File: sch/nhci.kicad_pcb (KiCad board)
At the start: 4 copper layers, 70 parts, among them IC1 74LVC8T245RHLRG4, IC2 74LVC8T245RHLRG4, IC3 74LVC8T245RHLRG4, IC4 74LVC8T245RHLRG4, IC5 74LVC8T245RHLRG4, IC6 MAX3421EEHJ+, IC7 LT3030IFE#TRPBF, J1 CLP-105-02-F-D, SW1 SW_Push_Open, U1 PCMCIA_BOARD, U2 iCE40-HX8K-CT256, U3 N25Q032A13EF440F, U4 LM3526M-H, Y1 ECS-5032MV-120-BM-TR

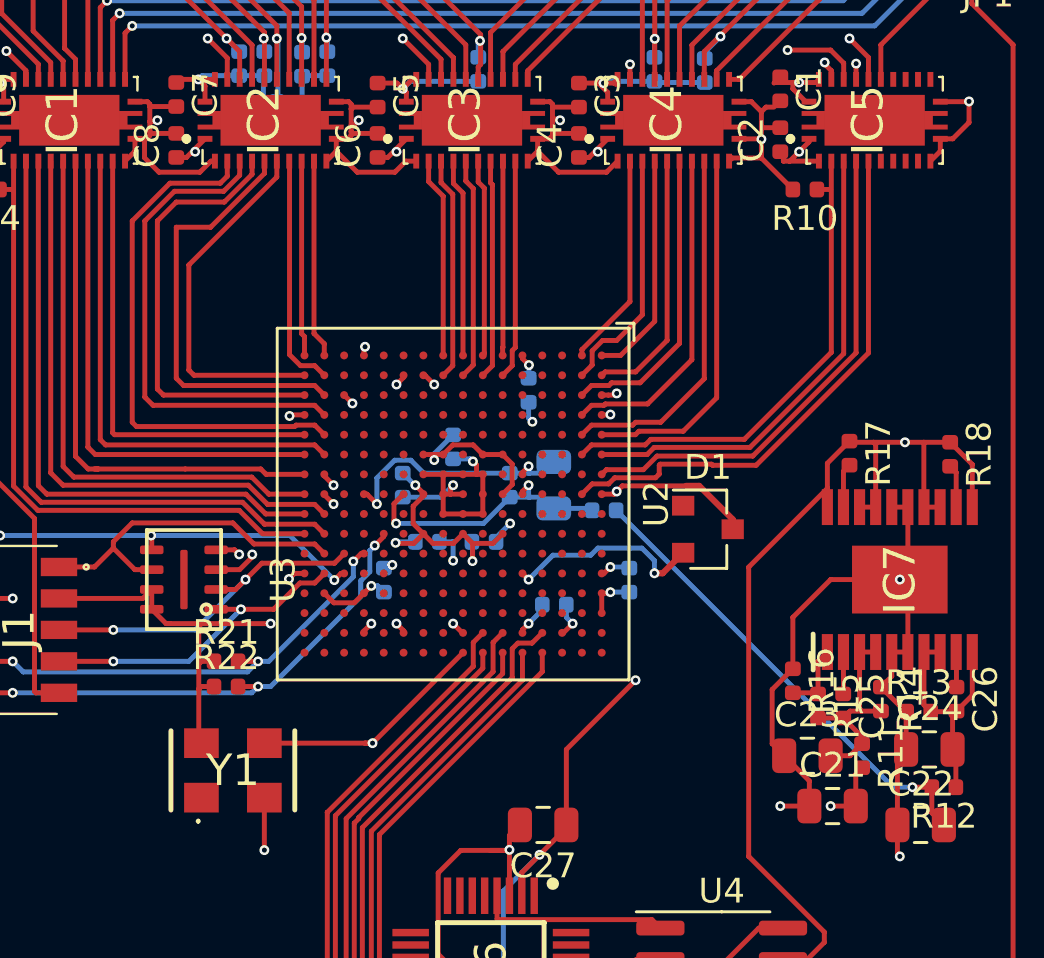
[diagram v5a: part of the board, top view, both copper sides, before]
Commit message: VCC is 1V2 not 3V3
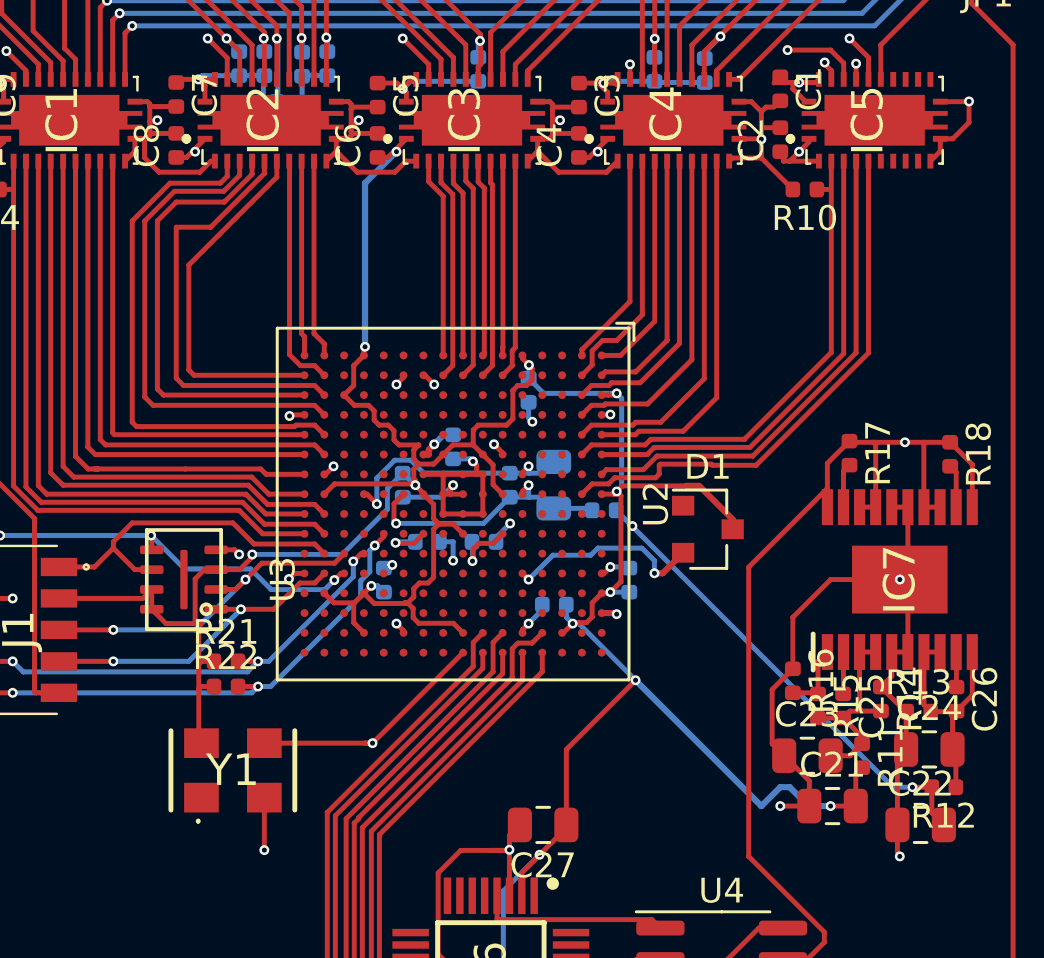
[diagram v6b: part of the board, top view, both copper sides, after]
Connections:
- C18 pad 1: +3V3 -> +1V2
- C19 pad 1: +3V3 -> +1V2
- C20 pad 1: +3V3 -> +1V2
- U2 pad A14: +3V3 -> +1V2
- U2 pad F10: +3V3 -> +1V2
- U2 pad F6: +3V3 -> +1V2
- U2 pad K10: +3V3 -> +1V2
- U2 pad K6: +3V3 -> +1V2
- U2 pad L2: +3V3 -> +1V2
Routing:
- net +3V3: track 137.3 -> 178.8 mm, vias 27 -> 18
- net +1V2: track 19.1 -> 27.4 mm, vias 1 -> 8
- added copper zone on In2.Cu, net +1V2
- removed copper zone on In2.Cu, net +3V3

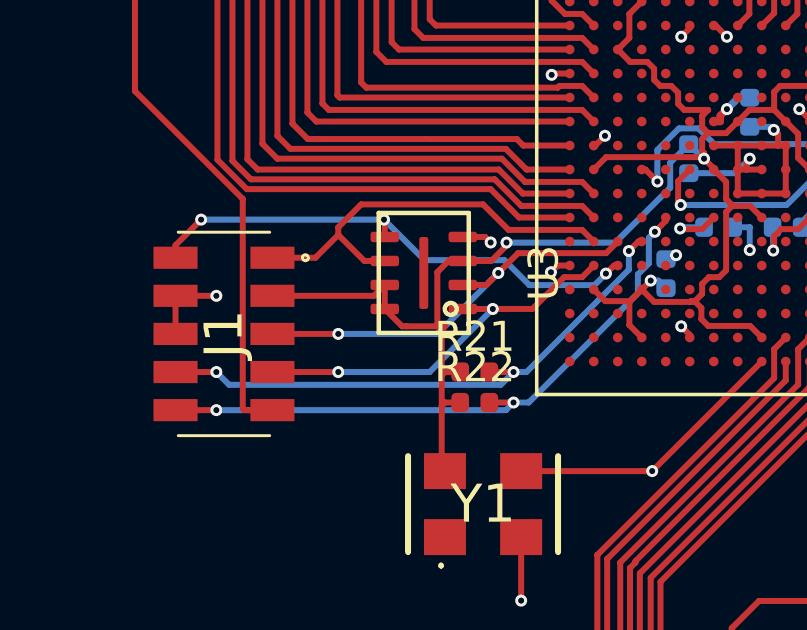
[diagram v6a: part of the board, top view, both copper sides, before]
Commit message: Add recommended SPI pullups
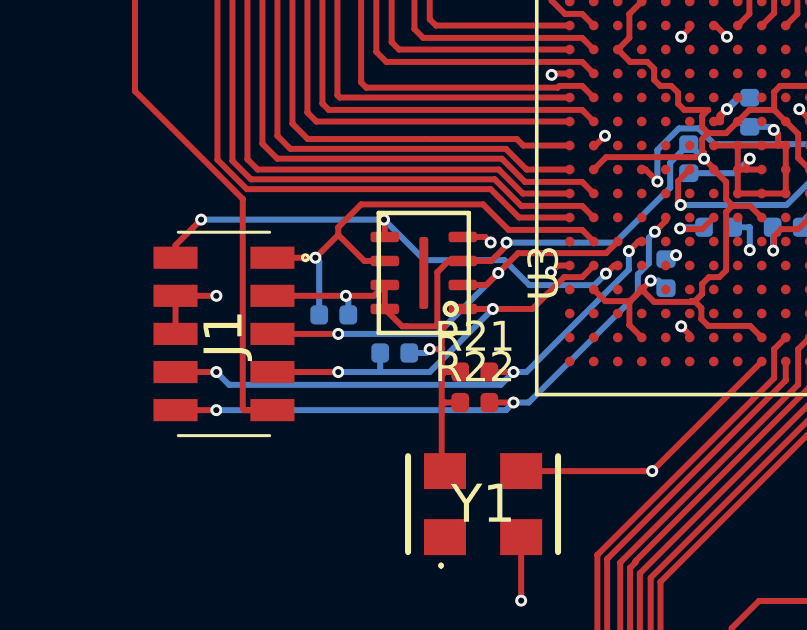
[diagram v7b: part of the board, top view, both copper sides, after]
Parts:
- added R25: 10k, Resistor_SMD:R_0402_1005Metric, B.Cu at (51.4, 128.9)
- added R26: 10k, Resistor_SMD:R_0402_1005Metric, B.Cu at (53.4, 130.2)
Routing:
- net Net-(J1-Pad1): track 14.0 -> 16.0 mm, vias 0 -> 1
- net +3V3: track 178.8 -> 180.6 mm, vias 18 -> 20
- net Net-(J1-Pad7): track 13.2 -> 13.8 mm
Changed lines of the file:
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@@
     (thickness 1.6)
     (drawings 0)
-    (tracks 1274)
+    (tracks 1289)
     (zones 0)
-    (modules 70)
+    (modules 72)
     (nets 370)
   )
@@
     (add_net U_SS)
   )
+  (module Resistor_SMD:R_0402_1005Metric (layer B.Cu)
+    (at 53.444 130.175)
+    (descr "Resistor SMD 0402 (1005 Metric), square (rectangular) end terminal, IPC_7351 nominal, (Body size source: http://www.tortai-tech.com/upload/download/2011102023233369053.pdf), generated with kicad-footprint-generator")
+    (tags resistor)
+    (attr smd)
+    (fp_text reference R26 (at 0 1.17) (layer B.SilkS)
+      (effects (font (size 1 1) (thickness 0.15)) (justify mirror))
+    )
+    (fp_text value 10k (at 0 -1.17) (layer B.Fab)
+      (effects (font (size 1 1) (thickness 0.15)) (justify mirror))
+    )
+    (fp_text user %R (at 0 0) (layer B.Fab)
+      (effects (font (size 0.25 0.25) (thickness 0.04)) (justify mirror))
+    )
+    (fp_line (start -0.5 -0.25) (end -0.5 0.25) (layer B.Fab) (width 0.1))
+    (fp_line (start -0.5 0.25) (end 0.5 0.25) (layer B.Fab) (width 0.1))
+    (fp_line (start 0.5 0.25) (end 0.5 -0.25) (layer B.Fab) (width 0.1))
+    (fp_line (start 0.5 -0.25) (end -0.5 -0.25) (layer B.Fab) (width 0.1))
+    (fp_line (start -0.93 -0.47) (end -0.93 0.47) (layer B.CrtYd) (width 0.05))
+    (fp_line (start -0.93 0.47) (end 0.93 0.47) (layer B.CrtYd) (width 0.05))
+    (fp_line (start 0.93 0.47) (end 0.93 -0.47) (layer B.CrtYd) (width 0.05))
+    (fp_line (start 0.93 -0.47) (end -0.93 -0.47) (layer B.CrtYd) (width 0.05))
+    (pad 2 smd roundrect (at 0.485 0) (size 0.59 0.64) (layers B.Cu B.Paste B.Mask) (roundrect_rratio 0.25)
+      (net 102 +3V3))
+    (pad 1 smd roundrect (at -0.485 0) (size 0.59 0.64) (layers B.Cu B.Paste B.Mask) (roundrect_rratio 0.25)
+      (net 350 "Net-(J1-Pad7)"))
+    (model ${KISYS3DMOD}/Resistor_SMD.3dshapes/R_0402_1005Metric.wrl
+      (at (xyz 0 0 0))
+      (scale (xyz 1 1 1))
+      (rotate (xyz 0 0 0))
+    )
+  )
+  (module Resistor_SMD:R_0402_1005Metric (layer B.Cu)
+    (at 51.412 128.905)
+    (descr "Resistor SMD 0402 (1005 Metric), square (rectangular) end terminal, IPC_7351 nominal, (Body size source: http://www.tortai-tech.com/upload/download/2011102023233369053.pdf), generated with kicad-footprint-generator")
+    (tags resistor)
+    (attr smd)
+    (fp_text reference R25 (at 0 1.17) (layer B.SilkS)
+      (effects (font (size 1 1) (thickness 0.15)) (justify mirror))
+    )
+    (fp_text value 10k (at 0 -1.17) (layer B.Fab)
+      (effects (font (size 1 1) (thickness 0.15)) (justify mirror))
+    )
+    (fp_text user %R (at 0 0) (layer B.Fab)
+      (effects (font (size 0.25 0.25) (thickness 0.04)) (justify mirror))
+    )
+    (fp_line (start -0.5 -0.25) (end -0.5 0.25) (layer B.Fab) (width 0.1))
+    (fp_line (start -0.5 0.25) (end 0.5 0.25) (layer B.Fab) (width 0.1))
+    (fp_line (start 0.5 0.25) (end 0.5 -0.25) (layer B.Fab) (width 0.1))
+    (fp_line (start 0.5 -0.25) (end -0.5 -0.25) (layer B.Fab) (width 0.1))
+    (fp_line (start -0.93 -0.47) (end -0.93 0.47) (layer B.CrtYd) (width 0.05))
+    (fp_line (start -0.93 0.47) (end 0.93 0.47) (layer B.CrtYd) (width 0.05))
+    (fp_line (start 0.93 0.47) (end 0.93 -0.47) (layer B.CrtYd) (width 0.05))
+    (fp_line (start 0.93 -0.47) (end -0.93 -0.47) (layer B.CrtYd) (width 0.05))
+    (pad 2 smd roundrect (at 0.485 0) (size 0.59 0.64) (layers B.Cu B.Paste B.Mask) (roundrect_rratio 0.25)
+      (net 102 +3V3))
+    (pad 1 smd roundrect (at -0.485 0) (size 0.59 0.64) (layers B.Cu B.Paste B.Mask) (roundrect_rratio 0.25)
+      (net 353 "Net-(J1-Pad1)"))
+    (model ${KISYS3DMOD}/Resistor_SMD.3dshapes/R_0402_1005Metric.wrl
+      (at (xyz 0 0 0))
+      (scale (xyz 1 1 1))
+      (rotate (xyz 0 0 0))
+    )
+  )
   (module Package_TO_SOT_SMD:SOT-23 (layer F.Cu)
     (at 75.565 125.476)
@@
   (segment (start 55.118 134.112) (end 55.00999 134.00399) (width 0.2) (layer F.Cu) (net 102))
   (segment (start 52.75 128.27) (end 53.112 127.908) (width 0.2) (layer F.Cu) (net 102))
-  (segment (start 49.367 128.27) (end 52.75 128.27) (width 0.2) (layer F.Cu) (net 102))
   (segment (start 55.118 130.81) (end 55.00999 130.91801) (width 0.2) (layer F.Cu) (net 102))
   (segment (start 55.626 130.81) (end 55.118 130.81) (width 0.2) (layer F.Cu) (net 102))
-  (segment (start 55.00999 130.91801) (end 55.00999 129.39401) (width 0.2) (layer F.Cu) (net 102))
   (segment (start 55.626 131.826) (end 55.118 131.826) (width 0.2) (layer F.Cu) (net 102))
   (segment (start 55.118 131.826) (end 55.00999 131.93401) (width 0.2) (layer F.Cu) (net 102))
@@
   (segment (start 70.358 129.286) (end 70.104 129.286) (width 0.2) (layer B.Cu) (net 102))
   (segment (start 72.644 131.572) (end 70.358 129.286) (width 0.2) (layer B.Cu) (net 102))
+  (via (at 51.816 128.27) (size 0.4) (drill 0.2) (layers F.Cu B.Cu) (net 102))
+  (segment (start 51.897 128.351) (end 51.816 128.27) (width 0.2) (layer B.Cu) (net 102))
+  (segment (start 51.897 128.905) (end 51.897 128.351) (width 0.2) (layer B.Cu) (net 102))
+  (segment (start 49.367 128.27) (end 51.816 128.27) (width 0.2) (layer F.Cu) (net 102))
+  (segment (start 51.816 128.27) (end 52.75 128.27) (width 0.2) (layer F.Cu) (net 102))
+  (via (at 54.61 130.048) (size 0.4) (drill 0.2) (layers F.Cu B.Cu) (net 102))
+  (segment (start 53.929 130.175) (end 54.483 130.175) (width 0.2) (layer B.Cu) (net 102))
+  (segment (start 54.483 130.175) (end 54.61 130.048) (width 0.2) (layer B.Cu) (net 102))
+  (segment (start 54.991 130.048) (end 55.00999 130.02901) (width 0.2) (layer F.Cu) (net 102))
+  (segment (start 54.61 130.048) (end 54.991 130.048) (width 0.2) (layer F.Cu) (net 102))
+  (segment (start 55.00999 130.91801) (end 55.00999 130.02901) (width 0.2) (layer F.Cu) (net 102))
+  (segment (start 55.00999 130.02901) (end 55.00999 129.39401) (width 0.2) (layer F.Cu) (net 102))
   (segment (start 80.518001 106.131998) (end 78.780002 106.131998) (width 0.2) (layer F.Cu) (net 103))
   (segment (start 81.046 107.316) (end 81.046 106.659997) (width 0.2) (layer F.Cu) (net 103))
@@
   (via (at 56.712 128.708) (size 0.4) (drill 0.2) (layers F.Cu B.Cu) (net 350))
   (segment (start 54.61 130.81) (end 56.712 128.708) (width 0.2) (layer B.Cu) (net 350))
-  (segment (start 51.562 130.81) (end 54.61 130.81) (width 0.2) (layer B.Cu) (net 350))
   (segment (start 55.712 128.708) (end 56.712 128.708) (width 0.2) (layer F.Cu) (net 350))
   (segment (start 56.712 128.708) (end 58.03124 128.708) (width 0.2) (layer F.Cu) (net 350))
+  (segment (start 52.959 130.175) (end 52.959 130.81) (width 0.2) (layer B.Cu) (net 350))
+  (segment (start 51.562 130.81) (end 52.959 130.81) (width 0.2) (layer B.Cu) (net 350))
+  (segment (start 52.959 130.81) (end 54.61 130.81) (width 0.2) (layer B.Cu) (net 350))
   (segment (start 60.490999 126.847001) (end 60.878 126.46) (width 0.2) (layer F.Cu) (net 351))
   (segment (start 60.490999 126.847001) (end 57.556999 126.847001) (width 0.2) (layer F.Cu) (net 351))
@@
   (segment (start 50.8 127) (end 51.562 126.238) (width 0.2) (layer F.Cu) (net 353))
   (segment (start 49.367 127) (end 50.8 127) (width 0.2) (layer F.Cu) (net 353))
+  (via (at 50.8 127) (size 0.4) (drill 0.2) (layers F.Cu B.Cu) (net 353))
+  (segment (start 50.927 128.905) (end 50.927 127.127) (width 0.2) (layer B.Cu) (net 353))
+  (segment (start 50.927 127.127) (end 50.8 127) (width 0.2) (layer B.Cu) (net 353))
   (via (at 61.248848 126.775662) (size 0.4) (drill 0.2) (layers F.Cu B.Cu) (net 354))
   (segment (start 61.678 126.46) (end 61.56451 126.46) (width 0.2) (layer F.Cu) (net 354))

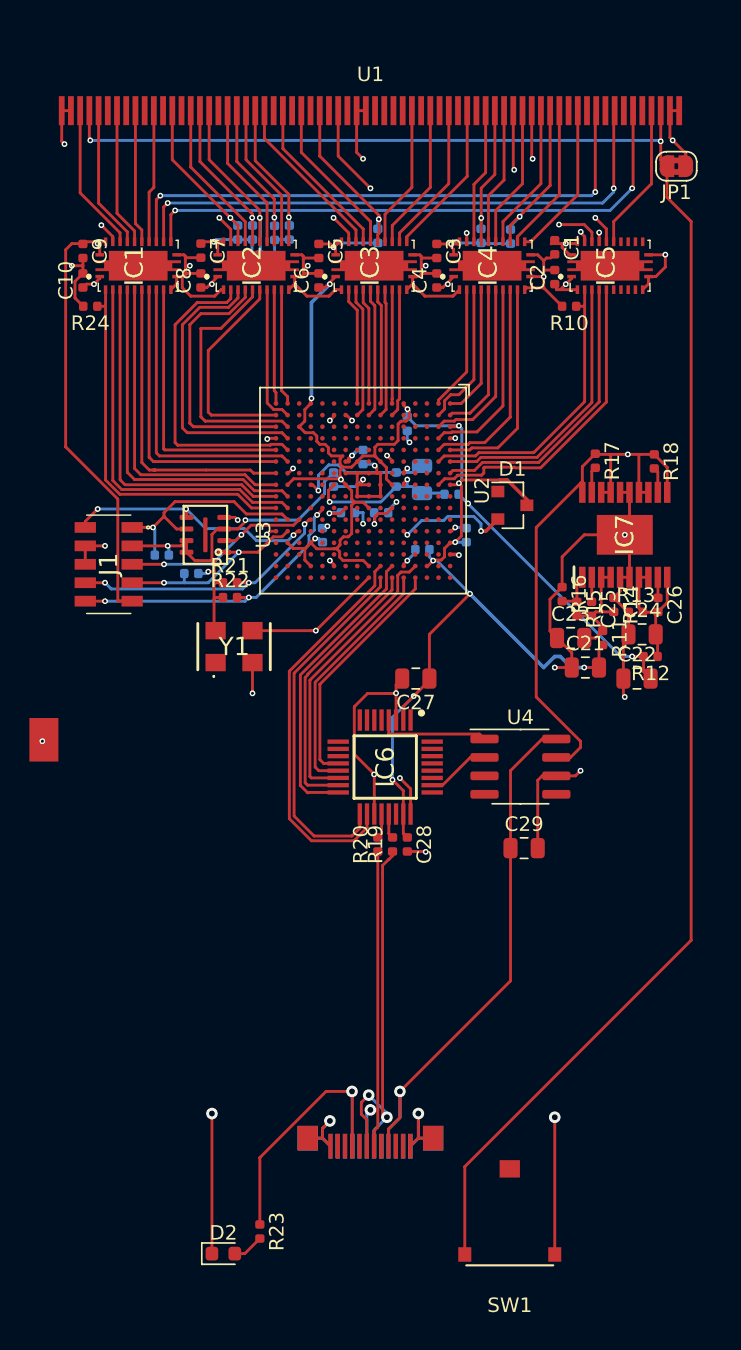
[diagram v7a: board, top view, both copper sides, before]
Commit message: Add edge cuts
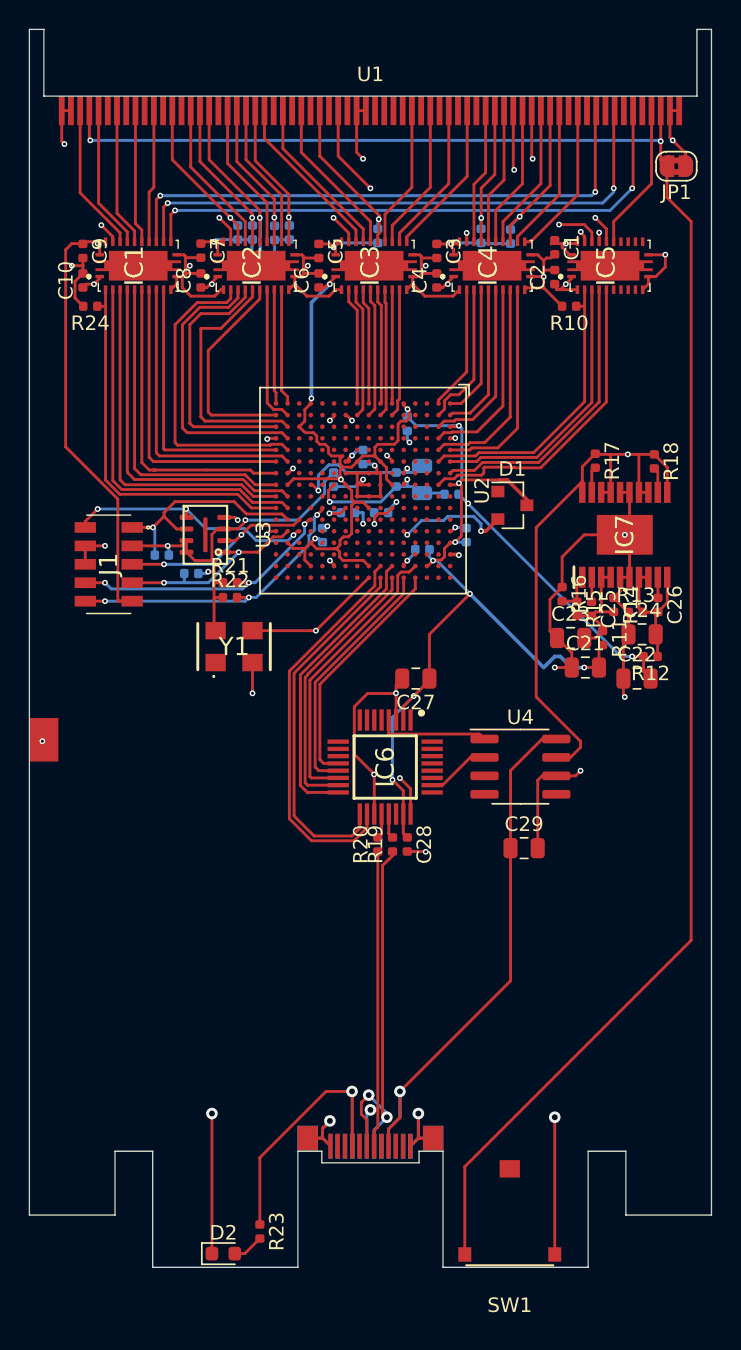
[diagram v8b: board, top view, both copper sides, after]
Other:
- board outline added: 47 x 85.3 mm
